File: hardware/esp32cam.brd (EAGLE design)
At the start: 33.5 x 34.6 mm, 45 parts, among them J1 MICRO_USB_B_HIROSE_ZX62-B-5PA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, J2 DM3AT-SF-PEJM5, Q1 HN1C01FU, U1 NJM11100, U2 NJM11100, U3 FT234XD-R, U4 NJM12888F, U5 ESP32-S3-WROOM-1-N16R2

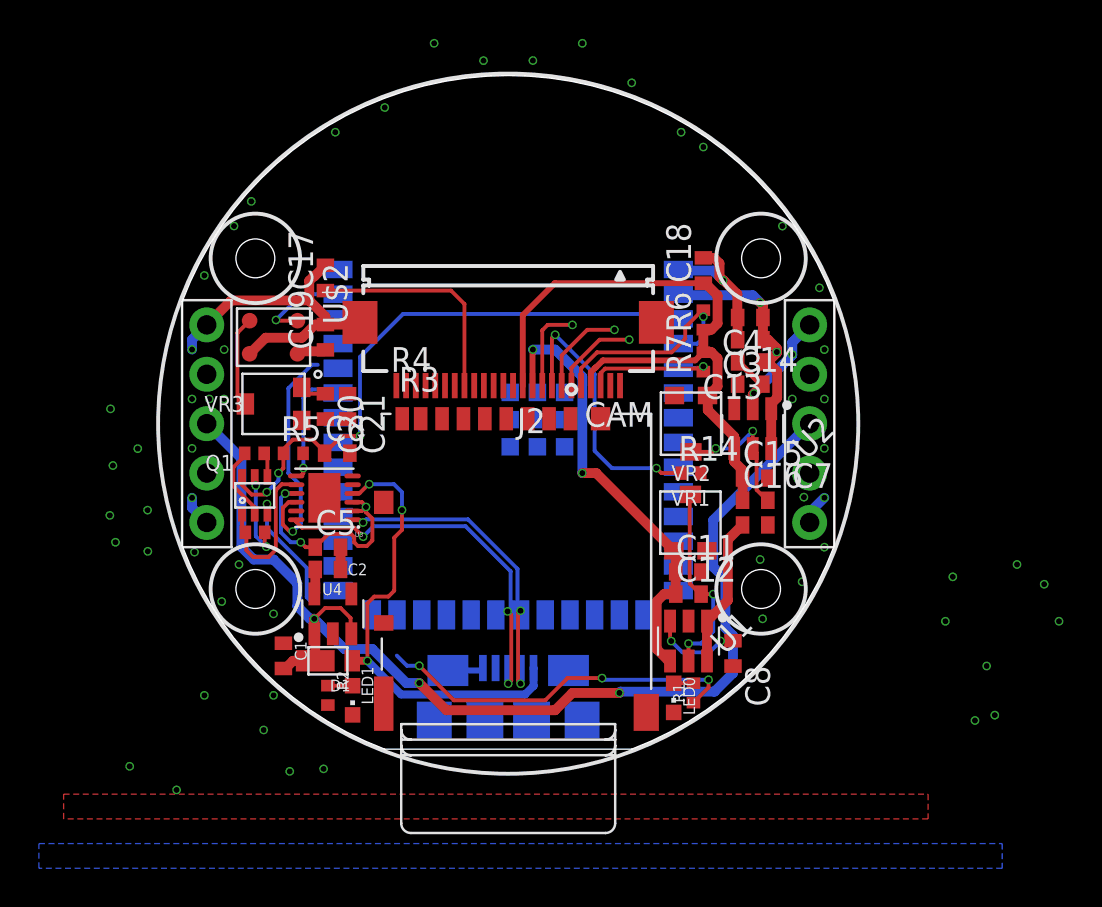
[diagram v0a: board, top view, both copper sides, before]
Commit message: べたGND前です。esp32のschはノータッチなのでここに上がってないです。よろしくお願いします。
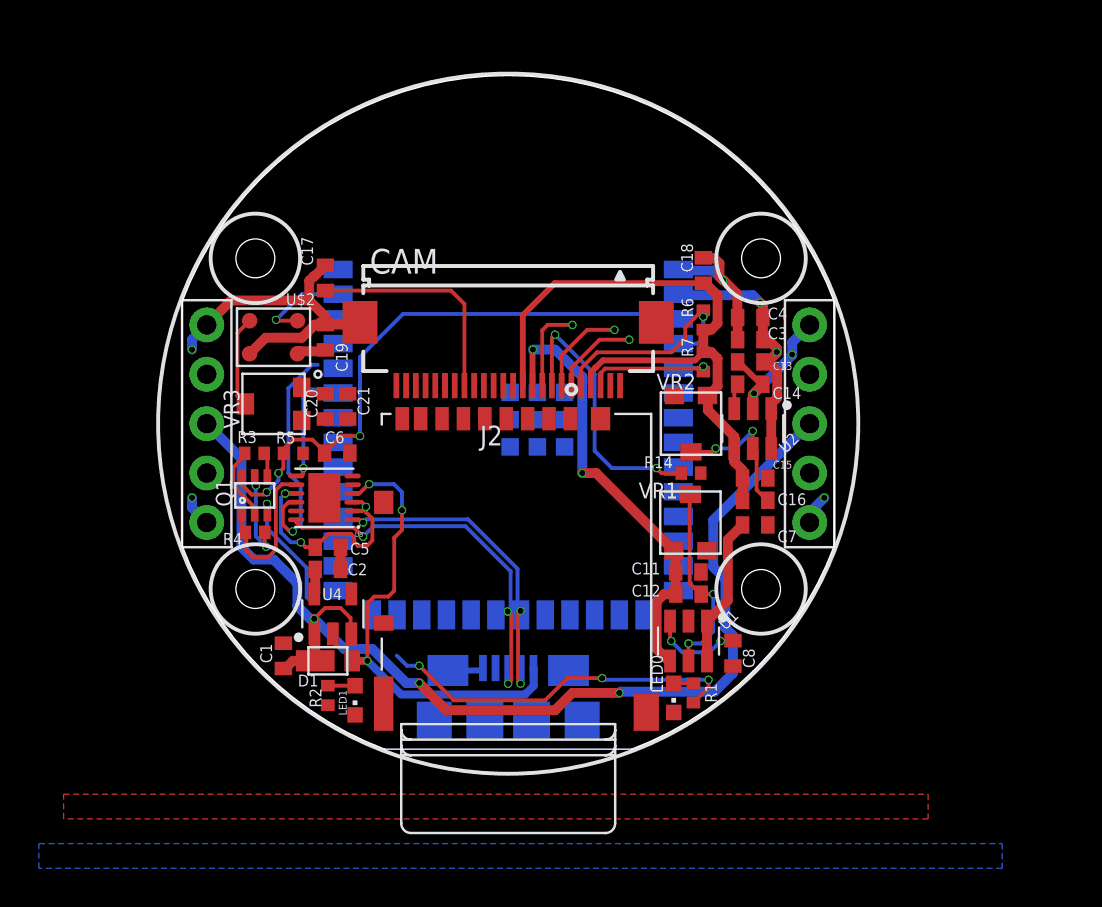
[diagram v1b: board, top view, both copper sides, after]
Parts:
- moved LED1 0.13 mm to (-7.87, -14.2)
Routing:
- net GND: vias 59 -> 6

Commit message: LiPoのだけできなかったのですが、それ以外のべたGND済のものです。
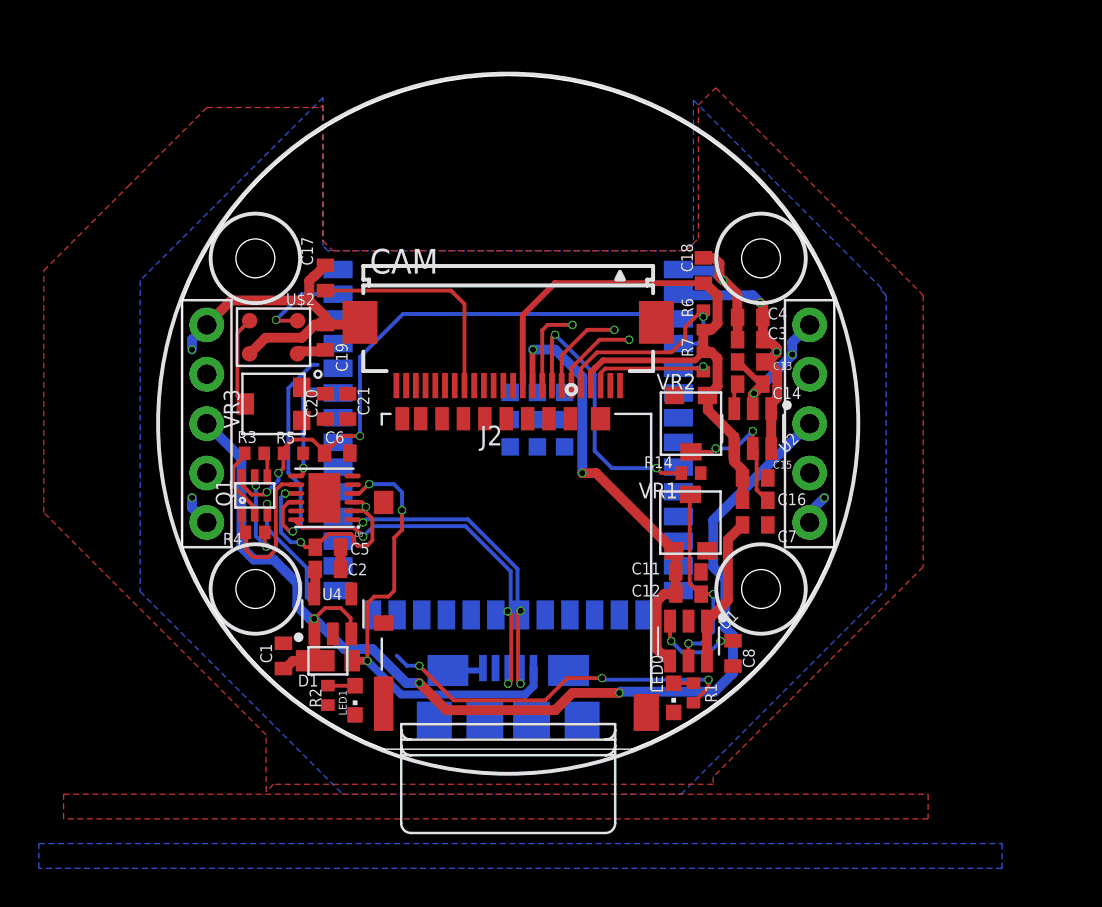
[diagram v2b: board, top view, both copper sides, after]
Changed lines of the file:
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@@
 <contactref element="J2" pad="P4"/>
 <contactref element="J2" pad="6"/>
+<polygon width="0.1524" layer="16">
+<vertex x="-9.525" y="9.144"/>
+<vertex x="-9.525" y="16.764"/>
+<vertex x="-18.923" y="7.366"/>
+<vertex x="-18.923" y="-8.636"/>
+<vertex x="-8.509" y="-19.05"/>
+<vertex x="8.89" y="-19.05"/>
+<vertex x="19.431" y="-8.509"/>
+<vertex x="19.431" y="6.604"/>
+<vertex x="19.177" y="6.858"/>
+<vertex x="19.177" y="6.985"/>
+<vertex x="9.525" y="16.637"/>
+<vertex x="9.525" y="9.271"/>
+<vertex x="9.144" y="8.89"/>
+<vertex x="-9.271" y="8.89"/>
+</polygon>
+<polygon width="0.1524" layer="1">
+<vertex x="-9.525" y="16.383"/>
+<vertex x="-9.525" y="9.398"/>
+<vertex x="-9.017" y="8.89"/>
+<vertex x="9.144" y="8.89"/>
+<vertex x="9.779" y="9.525"/>
+<vertex x="9.779" y="16.383"/>
+<vertex x="10.668" y="17.272"/>
+<vertex x="21.336" y="6.604"/>
+<vertex x="21.336" y="-7.366"/>
+<vertex x="10.541" y="-18.161"/>
+<vertex x="10.541" y="-18.542"/>
+<vertex x="-12.065" y="-18.542"/>
+<vertex x="-12.446" y="-18.923"/>
+<vertex x="-12.446" y="-16.002"/>
+<vertex x="-23.876" y="-4.572"/>
+<vertex x="-23.876" y="7.874"/>
+<vertex x="-19.558" y="12.192"/>
+<vertex x="-15.494" y="16.256"/>
+<vertex x="-9.652" y="16.256"/>
+</polygon>
+<wire x1="-9.451" y1="-3.8135" x2="-8.001" y2="-3.1385" width="0" layer="19" extent="1-1"/>
+<wire x1="9.911" y1="-7.623" x2="10.219" y2="-6.536" width="0" layer="19" extent="1-1"/>
+<wire x1="5.25" y1="1.957" x2="4.75" y2="0.254" width="0" layer="19" extent="1-1"/>
+<wire x1="9.271" y1="-10.1515" x2="9.911" y2="-7.623" width="0" layer="19" extent="1-1"/>
 <wire x1="-9.017" y1="-10.8035" x2="-11.557" y2="-11.288" width="0" layer="19" extent="1-1"/>
-<wire x1="-8.621" y1="-7.493" x2="-9.017" y2="-10.8035" width="0" layer="19" extent="1-1"/>
-<wire x1="-9.451" y1="-3.8135" x2="-8.621" y2="-6.35" width="0" layer="19" extent="1-1"/>
-<wire x1="-8.001" y1="-3.1385" x2="-9.451" y2="-3.8135" width="0" layer="19" extent="1-1"/>
-<wire x1="-8.1395" y1="-1.514" x2="-8.001" y2="-3.1385" width="0" layer="19" extent="1-1"/>
-<wire x1="-8.255" y1="0.239" x2="-8.1395" y2="-1.514" width="0" layer="19" extent="1-1"/>
-<wire x1="-9.398" y1="0.239" x2="-8.255" y2="0.239" width="0" layer="19" extent="1-1"/>
-<wire x1="-6.4" y1="-4.046" x2="-8.001" y2="-3.1385" width="0" layer="19" extent="1-1"/>
-<wire x1="-5.45" y1="0.254" x2="-8.255" y2="0.239" width="0" layer="19" extent="1-1"/>
-<wire x1="-2.3" y1="0.254" x2="-5.45" y2="0.254" width="0" layer="19" extent="1-1"/>
-<wire x1="-1.25" y1="1.957" x2="-2.3" y2="0.254" width="0" layer="19" extent="1-1"/>
-<wire x1="0.1" y1="1.607" x2="-1.25" y2="1.957" width="0" layer="19" extent="1-16"/>
-<wire x1="0.1" y1="0.207" x2="0.1" y2="1.607" width="0" layer="19" extent="16-16"/>
-<wire x1="0.1" y1="-1.193" x2="0.1" y2="0.207" width="0" layer="19" extent="16-16"/>
-<wire x1="1.5" y1="-1.193" x2="0.1" y2="-1.193" width="0" layer="19" extent="16-16"/>
-<wire x1="2.9" y1="-1.193" x2="1.5" y2="-1.193" width="0" layer="19" extent="16-16"/>
-<wire x1="2.9" y1="0.207" x2="2.9" y2="-1.193" width="0" layer="19" extent="16-16"/>
-<wire x1="2.9" y1="1.607" x2="2.9" y2="0.207" width="0" layer="19" extent="16-16"/>
-<wire x1="1.5" y1="1.607" x2="0.1" y2="1.607" width="0" layer="19" extent="16-16"/>
-<wire x1="1.5" y1="0.207" x2="0.1" y2="0.207" width="0" layer="19" extent="16-16"/>
-<wire x1="4.75" y1="0.254" x2="2.9" y2="0.207" width="0" layer="19" extent="1-16"/>
-<wire x1="5.25" y1="1.957" x2="4.75" y2="0.254" width="0" layer="19" extent="1-1"/>
-<wire x1="8.548" y1="1.45" x2="5.25" y2="1.957" width="0" layer="19" extent="1-1"/>
-<wire x1="11.796" y1="3.175" x2="8.548" y2="1.45" width="0" layer="19" extent="1-1"/>
-<wire x1="11.796" y1="4.318" x2="11.796" y2="3.175" width="0" layer="19" extent="1-1"/>
-<wire x1="11.78" y1="5.477" x2="11.796" y2="5.461" width="0" layer="19" extent="1-1"/>
+<wire x1="-8.621" y1="-6.35" x2="-9.451" y2="-3.8135" width="0" layer="19" extent="1-1"/>
 <wire x1="7.62" y1="5.207" x2="8.75" y2="7.927" width="0" layer="19" extent="1-16"/>
-<wire x1="13.35" y1="-2.794" x2="12.573" y2="0.7705" width="0" layer="19" extent="1-1"/>
-<wire x1="13.35" y1="-5.207" x2="13.35" y2="-2.794" width="0" layer="19" extent="1-1"/>
-<wire x1="15.5" y1="-5.08" x2="13.35" y2="-5.207" width="0" layer="19" extent="1-1"/>
-<wire x1="10.219" y1="-6.536" x2="13.35" y2="-5.207" width="0" layer="19" extent="1-1"/>
-<wire x1="9.911" y1="-7.623" x2="10.219" y2="-6.536" width="0" layer="19" extent="1-1"/>
-<wire x1="9.271" y1="-10.1515" x2="9.911" y2="-7.623" width="0" layer="19" extent="1-1"/>
-<wire x1="11.557" y1="-12.461" x2="9.271" y2="-10.1515" width="0" layer="19" extent="1-1"/>
-<wire x1="9.898" y1="-2.54" x2="13.35" y2="-2.794" width="0" layer="19" extent="1-1"/>
-<wire x1="8.509" y1="-14.847" x2="11.557" y2="-12.461" width="0" layer="19" extent="1-1"/>
-<wire x1="7.1" y1="-14.846" x2="8.509" y2="-14.847" width="0" layer="19" extent="1-1"/>
-<wire x1="3.8" y1="-15.24" x2="7.1" y2="-14.846" width="0" layer="19" extent="1-16"/>
-<wire x1="1.26046875" y1="-15.24" x2="3.78553125" y2="-15.24" width="0" layer="19" extent="16-16"/>
-<wire x1="-1.2" y1="-15.24" x2="1.2" y2="-15.24" width="0" layer="19" extent="16-16"/>
-<wire x1="-3.8" y1="-15.24" x2="-1.2" y2="-15.24" width="0" layer="19" extent="16-16"/>
-<wire x1="-3.1" y1="-12.69" x2="-3.8" y2="-15.24" width="0" layer="19" extent="16-16"/>
-<wire x1="3.1" y1="-12.69" x2="3.8" y2="-15.24" width="0" layer="19" extent="16-16"/>
-<wire x1="-6.4" y1="-14.396" x2="-3.8" y2="-15.24" width="0" layer="19" extent="1-16"/>
-<wire x1="-7.874" y1="-14.974" x2="-6.4" y2="-14.396" width="0" layer="19" extent="1-1"/>
-<wire x1="-9.398" y1="5.095" x2="-9.398" y2="0.239" width="0" layer="19" extent="1-1"/>
-<wire x1="-8.75" y1="7.927" x2="-9.398" y2="8.143" width="0" layer="19" extent="1-16"/>
-<wire x1="-15.5" y1="-5.08" x2="-9.451" y2="-3.8135" width="0" layer="19" extent="1-1"/>
 </signal>
 <signal name="USB_DM">

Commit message: シルクを調整
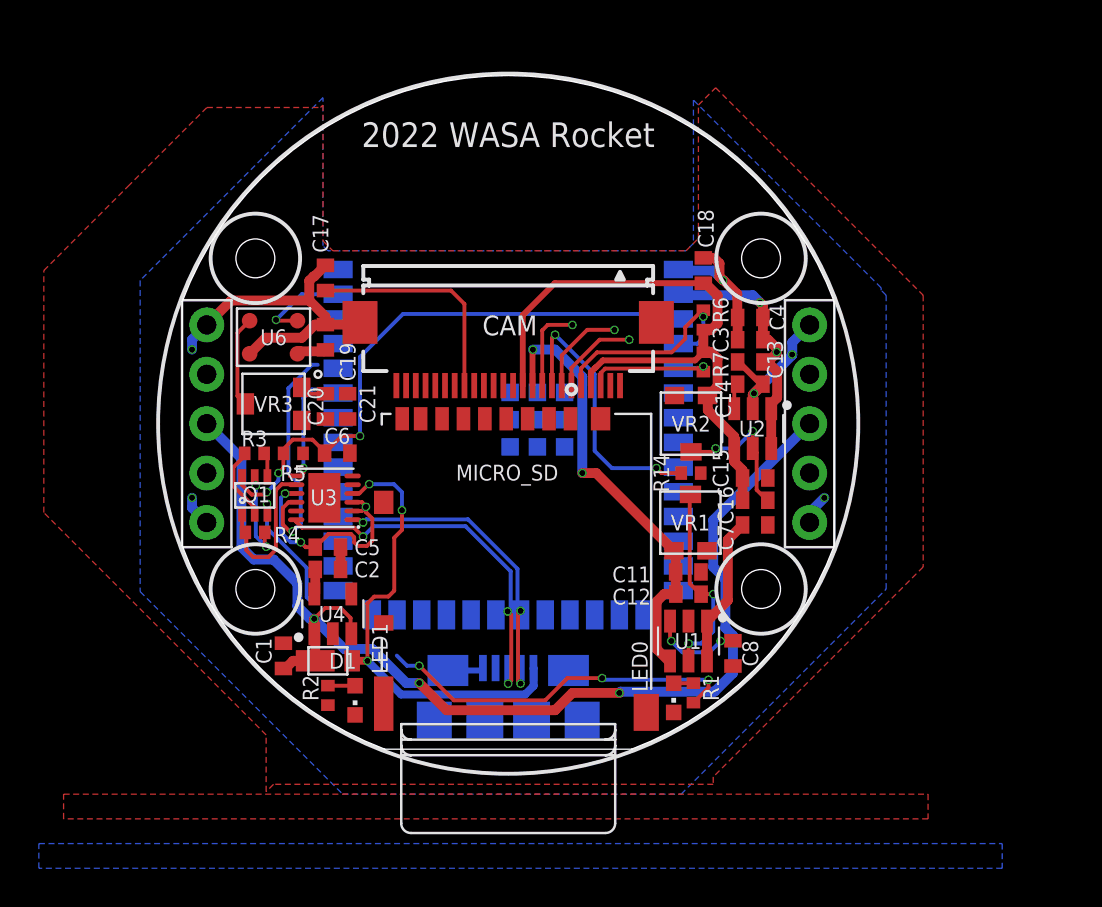
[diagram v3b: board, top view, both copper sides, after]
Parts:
- renumbered J2 to MICRO_SD, U$2 to U6, U5 to ESP32
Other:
- board text added: "TERES ESP32CAM Module"
- board text removed: "TERES Module"

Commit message: esp32cam途中
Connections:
- new net SPI0_CS: MICRO_SD.2
- new net SPI0_MISO: MICRO_SD.7
- new net SPI0_MOSI: MICRO_SD.3
- new net SPI0_SCK: MICRO_SD.5
- net CAM_RESET: now also ESP32.6
- net D0: now also ESP32.32
- net D1: now also ESP32.34
- net D2: now also ESP32.35
- net D3: now also ESP32.33
- net D4: now also ESP32.31
- net D5: now also ESP32.28
- net D6: now also ESP32.26
- net D7: now also ESP32.24
- net HSYNC: now also ESP32.8
- net PCLK: now also ESP32.30
- net VSYNC: now also ESP32.7
- net XCLK: now also ESP32.25
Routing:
- net D6: track 0.00 -> 24.6 mm, vias 0 -> 3
- net D7: track 0.00 -> 23.8 mm, vias 0 -> 3
- net XCLK: track 0.00 -> 21.7 mm, vias 0 -> 3
- net D5: track 0.00 -> 21.6 mm, vias 0 -> 3
- net D4: track 0.00 -> 16.2 mm, vias 0 -> 1
- net PCLK: track 11.6 -> 26.5 mm, vias 0 -> 3
- net D0: track 0.00 -> 12.2 mm, vias 0 -> 1
- net HSYNC: track 4.51 -> 14.6 mm
- net D3: track 0.00 -> 9.95 mm, vias 0 -> 1
- net D1: track 0.00 -> 9.08 mm, vias 0 -> 1
- net VSYNC: track 4.81 -> 12.2 mm
- net D2: track 0.00 -> 6.37 mm, vias 0 -> 1
- net CAM_RESET: track 4.49 -> 9.31 mm
- net USB_VCC: track 23.9 -> 27.3 mm
- net TRX: track 12.1 -> 14.6 mm
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
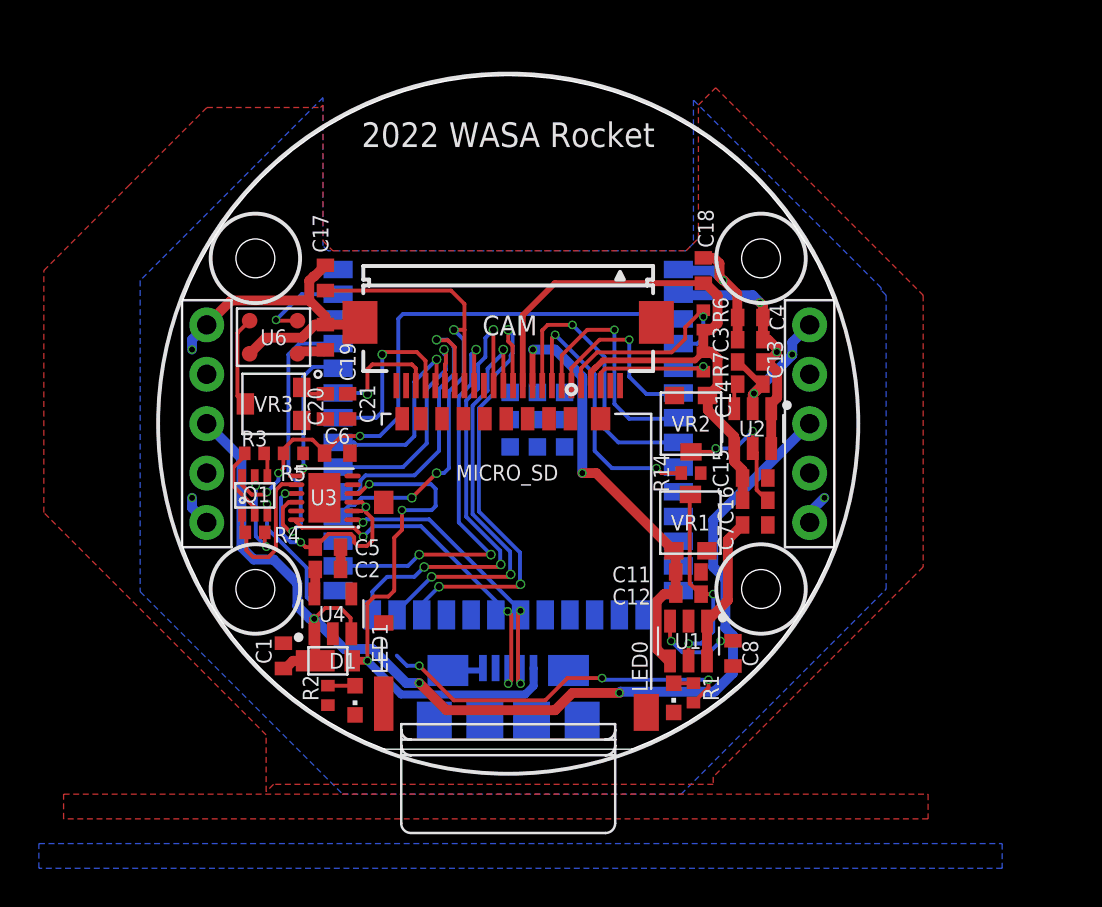
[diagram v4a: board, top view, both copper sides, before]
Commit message: 変更点:カメラモジュール・SDカード・LED1,2接続、未接続だったVDD、GNDの接続 一応完成したはずです。確認お願いします。
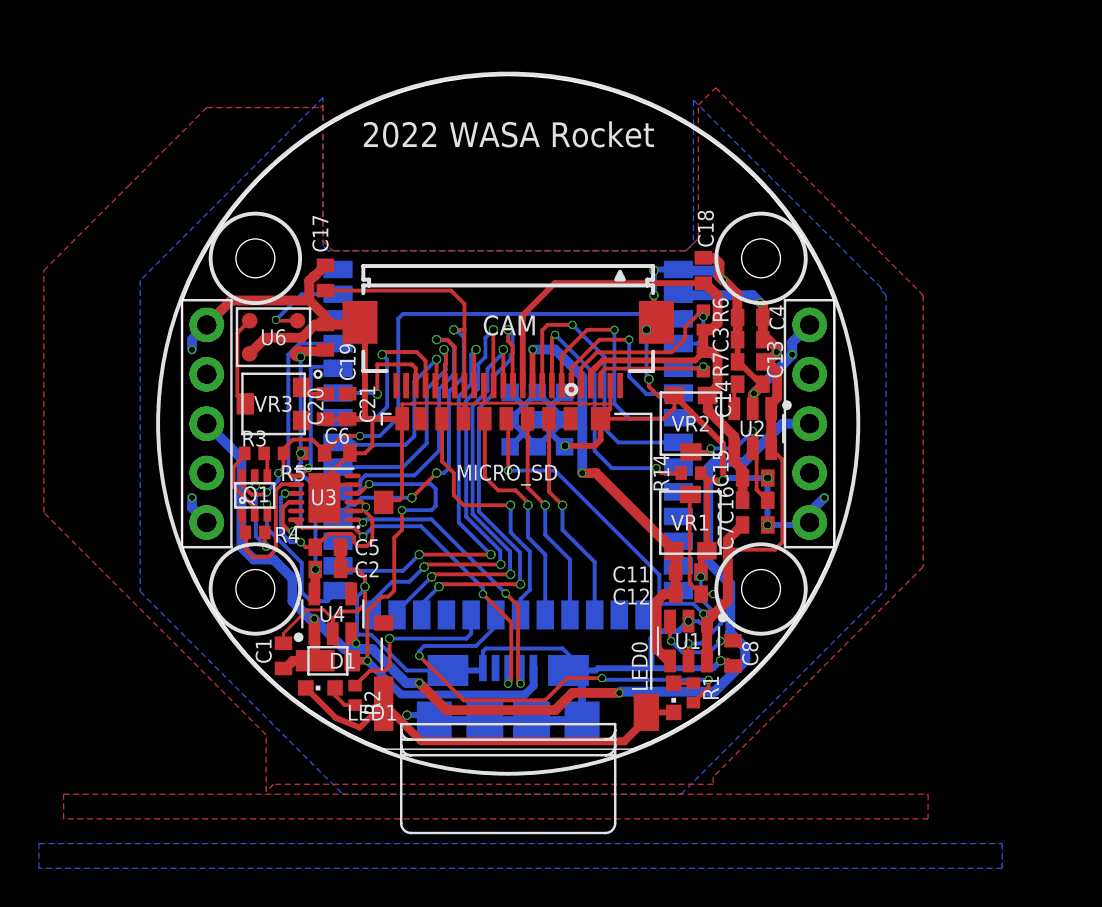
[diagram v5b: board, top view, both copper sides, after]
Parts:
- moved LED1 1.89 mm to (-9.65, -13.6), turned to 90 degrees
- moved R2 1.40 mm to (-7.87, -14.0), turned to 90 degrees
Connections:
- net LED0: now also ESP32.21
- net LED1: now also ESP32.22
- net SPI0_CS: now also ESP32.17
- net SPI0_MISO: now also ESP32.20
- net SPI0_MOSI: now also ESP32.18
- net SPI0_SCK: now also ESP32.19
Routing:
- net GND: track 39.6 -> 201.6 mm, vias 6 -> 19
- net VDD: track 24.0 -> 60.2 mm, vias 2 -> 7
- net SPI0_MISO: track 0.00 -> 13.6 mm, vias 0 -> 1
- net SPI0_SCK: track 0.00 -> 11.9 mm, vias 0 -> 1
- net SPI0_CS: track 0.00 -> 11.1 mm, vias 0 -> 1
- net SPI0_MOSI: track 0.00 -> 11.0 mm, vias 0 -> 1
- net LED1: track 0.00 -> 8.86 mm, vias 0 -> 1
- net LED0: track 19.0 -> 23.1 mm
- net IO0: track 6.45 -> 8.08 mm
- net V+: track 59.8 -> 60.1 mm, vias 3 -> 4

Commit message: 微調整
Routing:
- net VDD: track 60.2 -> 86.2 mm, vias 7 -> 10
- net D3: track 9.95 -> 10.7 mm
- net D7: track 23.8 -> 23.3 mm

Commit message: 若干修正
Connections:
- net RX0: now also ESP32.29
- net RX1: now also ESP32.10
- net SD: now also ESP32.23
- net TX0: now also ESP32.38
- net TX1: now also ESP32.9
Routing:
- net RX0: track 0.00 -> 19.2 mm, vias 0 -> 1
- net RX1: track 0.00 -> 11.4 mm, vias 0 -> 1
- net TX1: track 0.00 -> 9.55 mm
- net TX0: track 0.00 -> 7.93 mm
- net SD: track 0.00 -> 5.01 mm, vias 0 -> 1
- net RTX: track 7.50 -> 8.10 mm
